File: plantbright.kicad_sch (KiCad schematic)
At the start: 22 parts, among them J1 POWER OUT, J2 5V IN, Q1 AO3400A, Q2 AO3400A, Q3 AO3400A, Q4 AO3400A, Q5 AO3400A, SW1 USER 0, SW2 USER 1, U1 XIAO-ESP32-C6

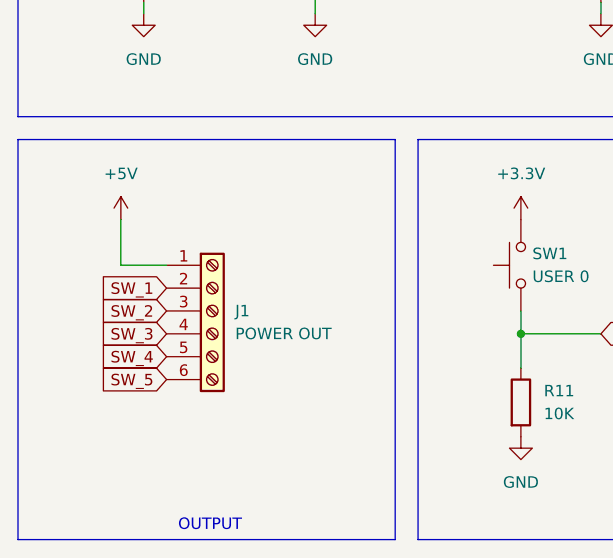
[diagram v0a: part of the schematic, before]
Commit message: Add current limiting resistors
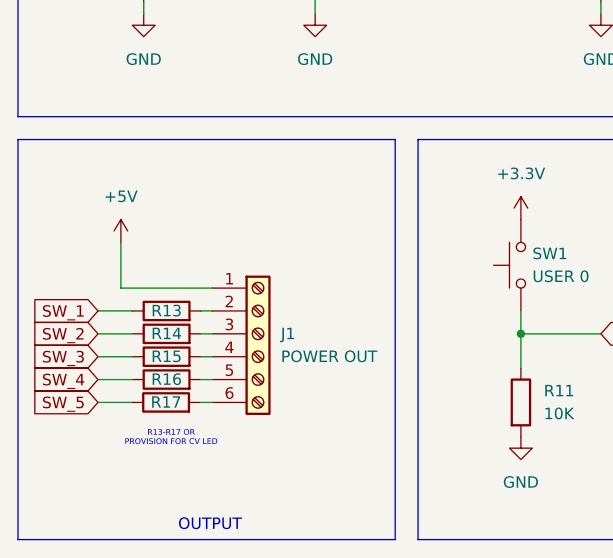
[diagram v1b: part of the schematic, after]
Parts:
- added R13, R14, R15, R16, R17: 0R, Resistor_SMD:R_1206_3216Metric_Pad1.30x1.75mm_HandSolder, symbol Device:R
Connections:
- net SW_1: now also R13.1; no longer J1.2 (Pin_2)
- net SW_2: now also R14.1; no longer J1.3 (Pin_3)
- net SW_3: now also R15.1; no longer J1.4 (Pin_4)
- net SW_4: now also R16.1; no longer J1.5 (Pin_5)
- net SW_5: now also R17.1; no longer J1.6 (Pin_6)
- new net: J1.2 (Pin_2), R13.2
- new net: J1.3 (Pin_3), R14.2
- new net: J1.4 (Pin_4), R15.2
- new net: J1.5 (Pin_5), R16.2
- new net: J1.6 (Pin_6), R17.2
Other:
- note added: "R13-R17 OR PROVISION FOR CV LED"
- moved on the sheet: J1

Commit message: Happy with layout, yay!
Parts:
- removed R12: 10K, Resistor_SMD:R_0805_2012Metric_Pad1.20x1.40mm_HandSolder, symbol Device:R
- removed SW2: USER 1, Button_Switch_THT:SW_PUSH_6mm, symbol Switch:SW_Push
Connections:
- net CH_3: no longer U1.4 (GPIO21/D3)
- net CH_4: now also U1.4 (GPIO21/D3); no longer U1.11 (GPIO18/D10/MOSI)
- net CH_5: now also U1.11 (GPIO18/D10/MOSI); no longer U1.10 (GPIO20/D9/MISO)
- net BTN_2: no longer names the net of U1.6 (GPIO23/D5/SCL)
- no-connect marks 3 -> 5
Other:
- note added: "BUTTON"
- note removed: "BUTTONS"

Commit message: Yay. Back to CV.
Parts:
- removed Q4: AO3400A, Package_TO_SOT_SMD:SOT-23, symbol Transistor_FET:AO3400A
- removed R17: 0R, Resistor_SMD:R_1206_3216Metric_Pad1.30x1.75mm_HandSolder, symbol Device:R
- removed R7: 100R, Resistor_SMD:R_0805_2012Metric_Pad1.20x1.40mm_HandSolder, symbol Device:R
- removed R8: 10K, Resistor_SMD:R_0805_2012Metric_Pad1.20x1.40mm_HandSolder, symbol Device:R
- J1: footprint Connector_JST:JST_XH_B6B-XH-A_1x06_P2.50mm_Vertical -> Connector_JST:JST_XH_B5B-XH-A_1x05_P2.50mm_Vertical; symbol Connector:Screw_Terminal_01x06 -> Connector:Screw_Terminal_01x05
- renumbered R13 to R10, R14 to R11, R15 to R12, R16 to R13, R9 to R7, R10 to R8, R11 to R9
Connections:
- net CH_5: no longer U1.11 (GPIO18/D10/MOSI)
- no-connect marks 5 -> 6
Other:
- note added: "POWER"
- note added: "R10-13 0R, OR SET FOR CV LED"
- note removed: "MOSFETs"
- note removed: "R13-R17 OR PROVISION FOR CV LED"
- moved on the sheet: J2

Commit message: Layout 'ings
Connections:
- net CH_5 is gone; now on net CH_4: R7.1, R8.1
- net SW_5 is gone; now on net SW_4: Q5.3 (D)
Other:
- moved on the sheet: J2, Q5, R7, R8
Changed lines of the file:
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@@
 	)
 	(junction
-		(at 132.08 35.56)
+		(at 82.55 73.66)
 		(diameter 0)
 		(color 0 0 0 0)
@@
 	(wire
 		(pts
-			(xy 151.13 26.67) (xy 151.13 30.48)
+			(xy 101.6 64.77) (xy 101.6 68.58)
 		)
 		(stroke
@@
 	(wire
 		(pts
-			(xy 82.55 74.93) (xy 86.36 74.93)
+			(xy 133.35 57.15) (xy 137.16 57.15)
 		)
 		(stroke
@@
 	(wire
 		(pts
-			(xy 82.55 72.39) (xy 82.55 67.31)
+			(xy 133.35 54.61) (xy 133.35 49.53)
 		)
 		(stroke
@@
 	(wire
 		(pts
-			(xy 140.97 35.56) (xy 143.51 35.56)
+			(xy 91.44 73.66) (xy 93.98 73.66)
 		)
 		(stroke
@@
 	(wire
 		(pts
-			(xy 82.55 81.28) (xy 82.55 74.93)
+			(xy 133.35 63.5) (xy 133.35 57.15)
 		)
 		(stroke
@@
 	(wire
 		(pts
-			(xy 86.36 72.39) (xy 82.55 72.39)
+			(xy 137.16 54.61) (xy 133.35 54.61)
 		)
 		(stroke
@@
 	(wire
 		(pts
-			(xy 132.08 38.1) (xy 132.08 35.56)
+			(xy 82.55 76.2) (xy 82.55 73.66)
 		)
 		(stroke
@@
 	(wire
 		(pts
-			(xy 151.13 40.64) (xy 151.13 46.99)
+			(xy 101.6 78.74) (xy 101.6 85.09)
 		)
 		(stroke
@@
 	(wire
 		(pts
-			(xy 127 35.56) (xy 132.08 35.56)
+			(xy 77.47 73.66) (xy 82.55 73.66)
 		)
 		(stroke
@@
 	(wire
 		(pts
-			(xy 132.08 45.72) (xy 132.08 46.99)
+			(xy 82.55 83.82) (xy 82.55 85.09)
 		)
 		(stroke
@@
 	(wire
 		(pts
-			(xy 132.08 35.56) (xy 133.35 35.56)
+			(xy 82.55 73.66) (xy 83.82 73.66)
 		)
 		(stroke
@@
 		)
 	)
-	(global_label "CH_5"
+	(global_label "CH_4"
 		(shape input)
-		(at 127 35.56 180)
+		(at 77.47 73.66 180)
 		(fields_autoplaced yes)
 		(effects
@@
 		)
 		(property "Intersheetrefs" "${INTERSHEET_REFS}"
-			(at 119.2372 35.56 0)
+			(at 69.7072 73.66 0)
 			(effects
 				(font
@@
 		)
 	)
-	(global_label "SW_5"
+	(global_label "SW_4"
 		(shape input)
-		(at 151.13 26.67 90)
+		(at 101.6 64.77 90)
 		(fields_autoplaced yes)
 		(effects
@@
 		)
 		(property "Intersheetrefs" "${INTERSHEET_REFS}"
-			(at 151.13 18.8468 90)
+			(at 101.6 56.9468 90)
 			(effects
 				(font
@@
 	(symbol
 		(lib_id "Connector:Screw_Terminal_01x02")
-		(at 91.44 72.39 0)
+		(at 142.24 54.61 0)
 		(unit 1)
 		(exclude_from_sim no)
@@
 		(fields_autoplaced yes)
 		(property "Reference" "J2"
-			(at 93.98 72.3899 0)
+			(at 144.78 54.6099 0)
 			(effects
 				(font
@@
 		)
 		(property "Value" "5V IN"
-			(at 93.98 74.9299 0)
+			(at 144.78 57.1499 0)
 			(effects
 				(font
@@
 		)
 		(property "Footprint" "Connector_JST:JST_XH_B2B-XH-A_1x02_P2.50mm_Vertical"
-			(at 91.44 72.39 0)
+			(at 142.24 54.61 0)
 			(effects
 				(font
@@
 		)
 		(property "Datasheet" "~"
-			(at 91.44 72.39 0)
+			(at 142.24 54.61 0)
 			(effects
 				(font
@@
 		)
 		(property "Description" "Generic screw terminal, single row, 01x02, script generated (kicad-library-utils/schlib/autogen/connector/)"
-			(at 91.44 72.39 0)
+			(at 142.24 54.61 0)
 			(effects
 				(font
@@
 	(symbol
 		(lib_id "Device:R")
-		(at 132.08 41.91 0)
+		(at 82.55 80.01 0)
 		(unit 1)
 		(exclude_from_sim no)
@@
 		(fields_autoplaced yes)
 		(property "Reference" "R8"
-			(at 134.62 40.6399 0)
+			(at 85.09 78.7399 0)
 			(effects
 				(font
@@
 		)
 		(property "Value" "10K"
-			(at 134.62 43.1799 0)
+			(at 85.09 81.2799 0)
 			(effects
 				(font
@@
 		)
 		(property "Footprint" "Resistor_SMD:R_0805_2012Metric_Pad1.20x1.40mm_HandSolder"
-			(at 130.302 41.91 90)
+			(at 80.772 80.01 90)
 			(effects
 				(font
@@
 		)
 		(property "Datasheet" "~"
-			(at 132.08 41.91 0)
+			(at 82.55 80.01 0)
 			(effects
 				(font
@@
 		)
 		(property "Description" "Resistor"
-			(at 132.08 41.91 0)
+			(at 82.55 80.01 0)
 			(effects
 				(font
@@
 	(symbol
 		(lib_id "power:GND")
-		(at 151.13 46.99 0)
+		(at 101.6 85.09 0)
 		(unit 1)
 		(exclude_from_sim no)
@@
 		(fields_autoplaced yes)
 		(property "Reference" "#PWR014"
-			(at 151.13 53.34 0)
+			(at 101.6 91.44 0)
 			(effects
 				(font
@@
 		)
 		(property "Value" "GND"
-			(at 151.13 52.07 0)
+			(at 101.6 90.17 0)
 			(effects
 				(font
@@
 		)
 		(property "Footprint" ""
-			(at 151.13 46.99 0)
+			(at 101.6 85.09 0)
 			(effects
 				(font
@@
 		)
 		(property "Datasheet" ""
-			(at 151.13 46.99 0)
+			(at 101.6 85.09 0)
 			(effects
 				(font
@@
 		)
 		(property "Description" "Power symbol creates a global label with name \"GND\" , ground"
-			(at 151.13 46.99 0)
+			(at 101.6 85.09 0)
 			(effects
 				(font
@@
 	(symbol
 		(lib_id "power:+5V")
-		(at 82.55 67.31 0)
+		(at 133.35 49.53 0)
 		(unit 1)
 		(exclude_from_sim no)
@@
 		(fields_autoplaced yes)
 		(property "Reference" "#PWR020"
-			(at 82.55 71.12 0)
+			(at 133.35 53.34 0)
 			(effects
 				(font
@@
 		)
 		(property "Value" "+5V"
-			(at 82.55 62.23 0)
+			(at 133.35 44.45 0)
 			(effects
 				(font
@@
 		)
 		(property "Footprint" ""
-			(at 82.55 67.31 0)
+			(at 133.35 49.53 0)
 			(effects
 				(font
@@
 		)
 		(property "Datasheet" ""
-			(at 82.55 67.31 0)
+			(at 133.35 49.53 0)
 			(effects
 				(font
@@
 		)
 		(property "Description" "Power symbol creates a global label with name \"+5V\""
-			(at 82.55 67.31 0)
+			(at 133.35 49.53 0)
 			(effects
 				(font
@@
 	(symbol
 		(lib_id "power:GND")
-		(at 132.08 46.99 0)
+		(at 82.55 85.09 0)
 		(unit 1)
 		(exclude_from_sim no)
@@
 		(fields_autoplaced yes)
 		(property "Reference" "#PWR012"
-			(at 132.08 53.34 0)
+			(at 82.55 91.44 0)
 			(effects
 				(font
@@
 		)
 		(property "Value" "GND"
-			(at 132.08 52.07 0)
+			(at 82.55 90.17 0)
 			(effects
 				(font
@@
 		)
 		(property "Footprint" ""
-			(at 132.08 46.99 0)
+			(at 82.55 85.09 0)
 			(effects
 				(font
@@
 		)
 		(property "Datasheet" ""
-			(at 132.08 46.99 0)
+			(at 82.55 85.09 0)
 			(effects
 				(font
@@
 		)
 		(property "Description" "Power symbol creates a global label with name \"GND\" , ground"
-			(at 132.08 46.99 0)
+			(at 82.55 85.09 0)
 			(effects
 				(font
@@
 	(symbol
 		(lib_id "power:GND")
-		(at 82.55 81.28 0)
+		(at 133.35 63.5 0)
 		(unit 1)
 		(exclude_from_sim no)
@@
 		(fields_autoplaced yes)
 		(property "Reference" "#PWR019"
-			(at 82.55 87.63 0)
+			(at 133.35 69.85 0)
 			(effects
 				(font
@@
 		)
 		(property "Value" "GND"
-			(at 82.55 86.36 0)
+			(at 133.35 68.58 0)
 			(effects
 				(font
@@
 		)
 		(property "Footprint" ""
-			(at 82.55 81.28 0)
+			(at 133.35 63.5 0)
 			(effects
 				(font
@@
 		)
 		(property "Datasheet" ""
-			(at 82.55 81.28 0)
+			(at 133.35 63.5 0)
 			(effects
 				(font
@@
 		)
 		(property "Description" "Power symbol creates a global label with name \"GND\" , ground"
-			(at 82.55 81.28 0)
+			(at 133.35 63.5 0)
 			(effects
 				(font
@@
 	(symbol
 		(lib_id "Device:R")
-		(at 137.16 35.56 90)
+		(at 87.63 73.66 90)
 		(unit 1)
 		(exclude_from_sim no)
@@
 		(fields_autoplaced yes)
 		(property "Reference" "R7"
-			(at 137.16 29.21 90)
+			(at 87.63 67.31 90)
 			(effects
 				(font
@@
 		)
 		(property "Value" "100R"
-			(at 137.16 31.75 90)
+			(at 87.63 69.85 90)
 			(effects
 				(font
@@
 		)
 		(property "Footprint" "Resistor_SMD:R_0805_2012Metric_Pad1.20x1.40mm_HandSolder"
-			(at 137.16 37.338 90)
+			(at 87.63 75.438 90)
 			(effects
 				(font
@@
 		)
 		(property "Datasheet" "~"
-			(at 137.16 35.56 0)
+			(at 87.63 73.66 0)
 			(effects
 				(font
@@
 		)
 		(property "Description" "Resistor"
-			(at 137.16 35.56 0)
+			(at 87.63 73.66 0)
 			(effects
 				(font
@@
 	(symbol
 		(lib_id "Transistor_FET:AO3400A")
-		(at 148.59 35.56 0)
+		(at 99.06 73.66 0)
 		(unit 1)
 		(exclude_from_sim no)
@@
 		(fields_autoplaced yes)
 		(property "Reference" "Q5"
-			(at 154.94 34.2899 0)
+			(at 105.41 72.3899 0)
 			(effects
 				(font
@@
 		)
 		(property "Value" "AO3400A"
-			(at 154.94 36.8299 0)
+			(at 105.41 74.9299 0)
 			(effects
 				(font
@@
 		)
 		(property "Footprint" "Package_TO_SOT_SMD:SOT-23"
-			(at 153.67 37.465 0)
+			(at 104.14 75.565 0)
 			(effects
 				(font
@@
 		)
 		(property "Datasheet" "http://www.aosmd.com/pdfs/datasheet/AO3400A.pdf"
-			(at 153.67 39.37 0)
+			(at 104.14 77.47 0)
 			(effects
 				(font
@@
 		)
 		(property "Description" "30V Vds, 5.7A Id, N-Channel MOSFET, SOT-23"
-			(at 148.59 35.56 0)
+			(at 99.06 73.66 0)
 			(effects
 				(font

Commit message: Switch to screw terminals
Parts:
- J1: footprint Connector_JST:JST_XH_B5B-XH-A_1x05_P2.50mm_Vertical -> TerminalBlock_Phoenix:TerminalBlock_Phoenix_MPT-0,5-5-2.54_1x05_P2.54mm_Horizontal
- J2: footprint Connector_JST:JST_XH_B2B-XH-A_1x02_P2.50mm_Vertical -> TerminalBlock_Phoenix:TerminalBlock_Phoenix_MPT-0,5-2-2.54_1x02_P2.54mm_Horizontal
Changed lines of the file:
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@@
 			)
 		)
-		(property "Footprint" "Connector_JST:JST_XH_B2B-XH-A_1x02_P2.50mm_Vertical"
+		(property "Footprint" "TerminalBlock_Phoenix:TerminalBlock_Phoenix_MPT-0,5-2-2.54_1x02_P2.54mm_Horizontal"
 			(at 142.24 54.61 0)
 			(effects
@@
 			)
 		)
-		(property "Footprint" "Connector_JST:JST_XH_B5B-XH-A_1x05_P2.50mm_Vertical"
+		(property "Footprint" "TerminalBlock_Phoenix:TerminalBlock_Phoenix_MPT-0,5-5-2.54_1x05_P2.54mm_Horizontal"
 			(at 44.45 120.65 0)
 			(effects

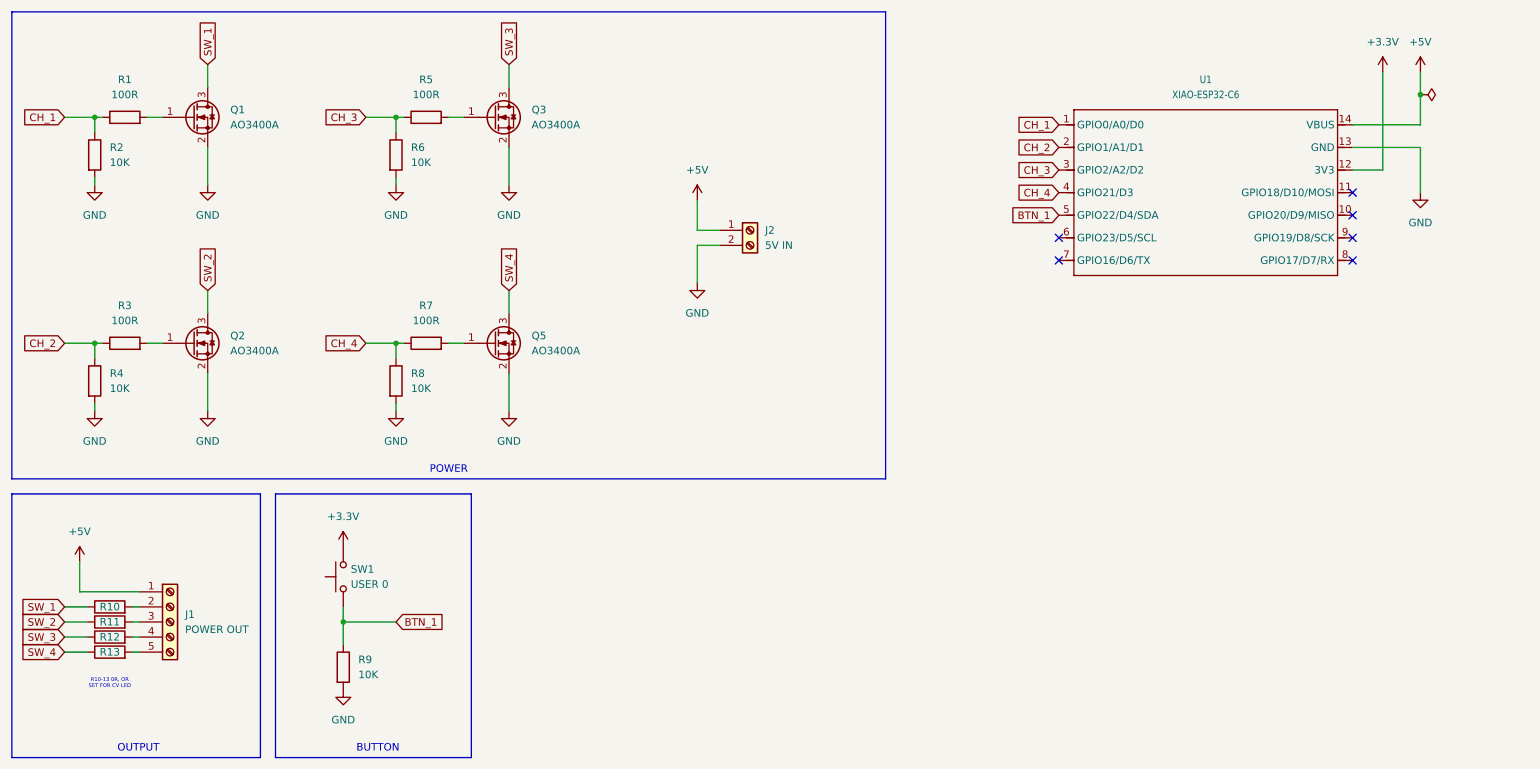
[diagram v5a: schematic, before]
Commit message: Switch to USB-C
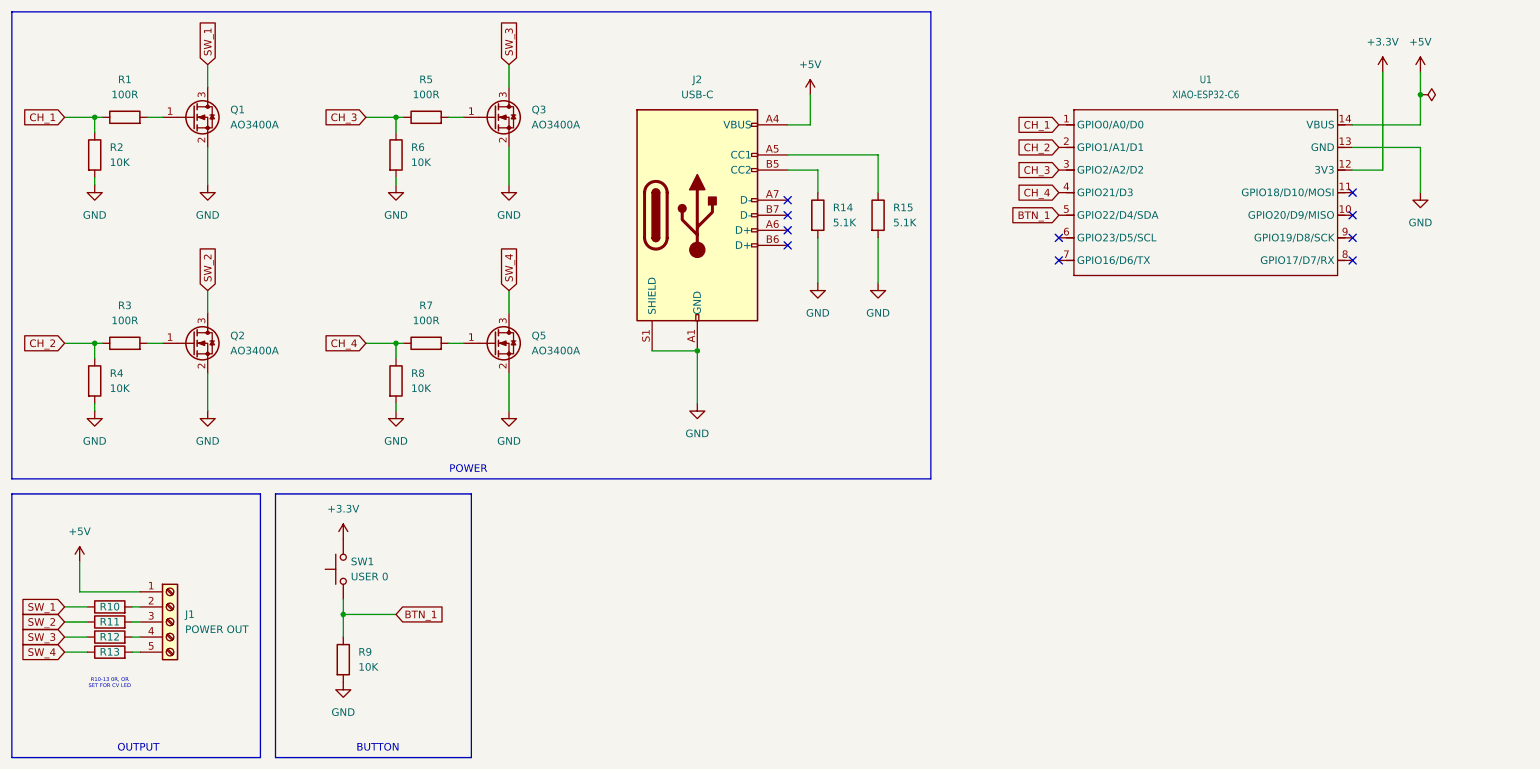
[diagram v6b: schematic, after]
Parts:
- removed J2: 5V IN, TerminalBlock_Phoenix:TerminalBlock_Phoenix_MPT-0,5-2-2.54_1x02_P2.54mm_Horizontal, symbol Connector:Screw_Terminal_01x02
- added J2: USB-C, Connector_USB:USB_C_Receptacle_HRO_TYPE-C-31-M-12, symbol Connector:USB_C_Receptacle_USB2.0_14P
- added R14, R15: 5.1K, Resistor_SMD:R_0805_2012Metric_Pad1.20x1.40mm_HandSolder, symbol Device:R
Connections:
- net +5V: now also J2.A4 (VBUS), J2.A9 (VBUS), J2.B4 (VBUS), J2.B9 (VBUS)
- net GND: now also J2.A1 (GND), J2.A12 (GND), J2.B1 (GND), J2.B12 (GND), J2.S1 (SHIELD), R14.2, R15.2
- new net: J2.B5 (CC2), R14.1
- new net: J2.A5 (CC1), R15.1
- no-connect marks 6 -> 10
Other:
- moved on the sheet: R9, SW1
